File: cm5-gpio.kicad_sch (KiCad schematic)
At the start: 13 parts

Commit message: power planes and sensor placement
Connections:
- net I2C2.SCL: now also CM5-1.28 (GPIO13)
- net I2C2.SDA: no longer CM5-1.28 (GPIO13)
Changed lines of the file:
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@@
 		)
 	)
-	(label "I2C2.SDA"
+	(label "I2C2.SCL"
 		(at 59.69 62.23 0)
 		(effects

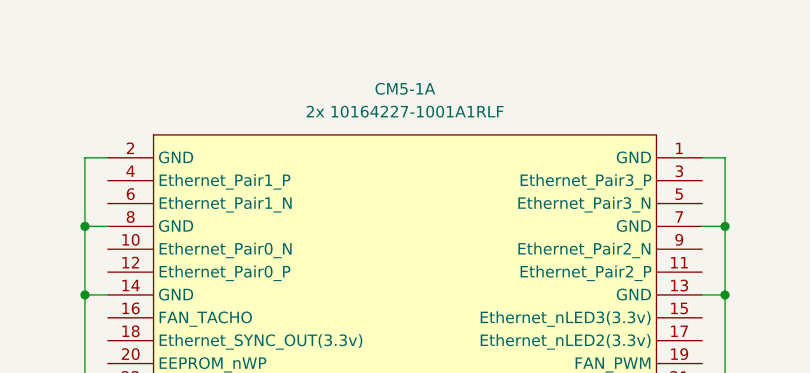
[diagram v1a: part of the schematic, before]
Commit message: redid gpio layout, removed one temp sensor, bom
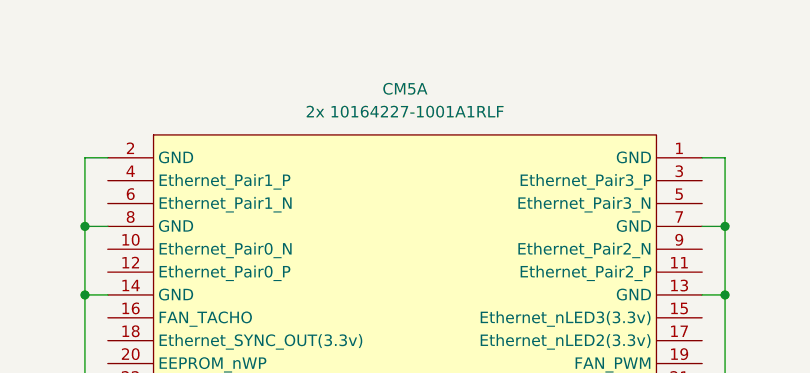
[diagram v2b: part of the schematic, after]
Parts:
- CM5: renamed from CM5-1; Manufacturer (none) -> Amphenol ICC (FCI); Manufacturer Product Number (none) -> 10164227-1001A1RLF
- D1: Field4 Digikey -> (none); Field5 LTST-S270KGKT -> (none); Field6 SML-A12M8TT86N -> (none); Field7 Rohm -> (none); Field8 650263301 -> (none); Manufacturer (none) -> Lite-On Inc.; Manufacturer Product Number (none) -> LTST-S270KGKT; Part Description Green 572nm LED Indication - Discrete 2.2V 2-SMD, No Lead -> (none)
- D2: Field4 Digikey -> (none); Field5 LTST-S270KGKT -> (none); Field6 SML-A12M8TT86N -> (none); Field7 Rohm -> (none); Field8 650263301 -> (none); Manufacturer (none) -> Lite-On Inc.; Manufacturer Product Number (none) -> LTST-S270KRKT; Part Description Green 572nm LED Indication - Discrete 2.2V 2-SMD, No Lead -> (none)
- R1, R10, R11, R12, R2, R9: Field4 Farnell -> (none); Manufacturer (none) -> Vishay Dale; Manufacturer Product Number (none) -> CRCW04022K20FKED; Part Description Resistor 2.2K M1005 1% 63mW -> (none)
- R3, R4: Field4 Farnell -> (none); Field5 9239235 -> (none); Field6 RK73H1ETTP1001F -> (none); Field7 KOA EUROPE GMBH -> (none); Field8 125049511 -> (none); Manufacturer (none) -> YAGEO; Manufacturer Product Number (none) -> RC0402JR-071KL; Part Description Resistor 1K M1005 1% 63mW -> (none)
- TP16, TP17: now left out of the parts list
